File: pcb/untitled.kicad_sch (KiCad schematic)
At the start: 66 parts, among them J1 00222-32051, J10 0022-232021, J2 0022-232021, J3 0022-232041, J8 00222-32051, Q1 SI7465DP-T1-E3, U2 MP26123DR-LF-Z, U3 TPS63070

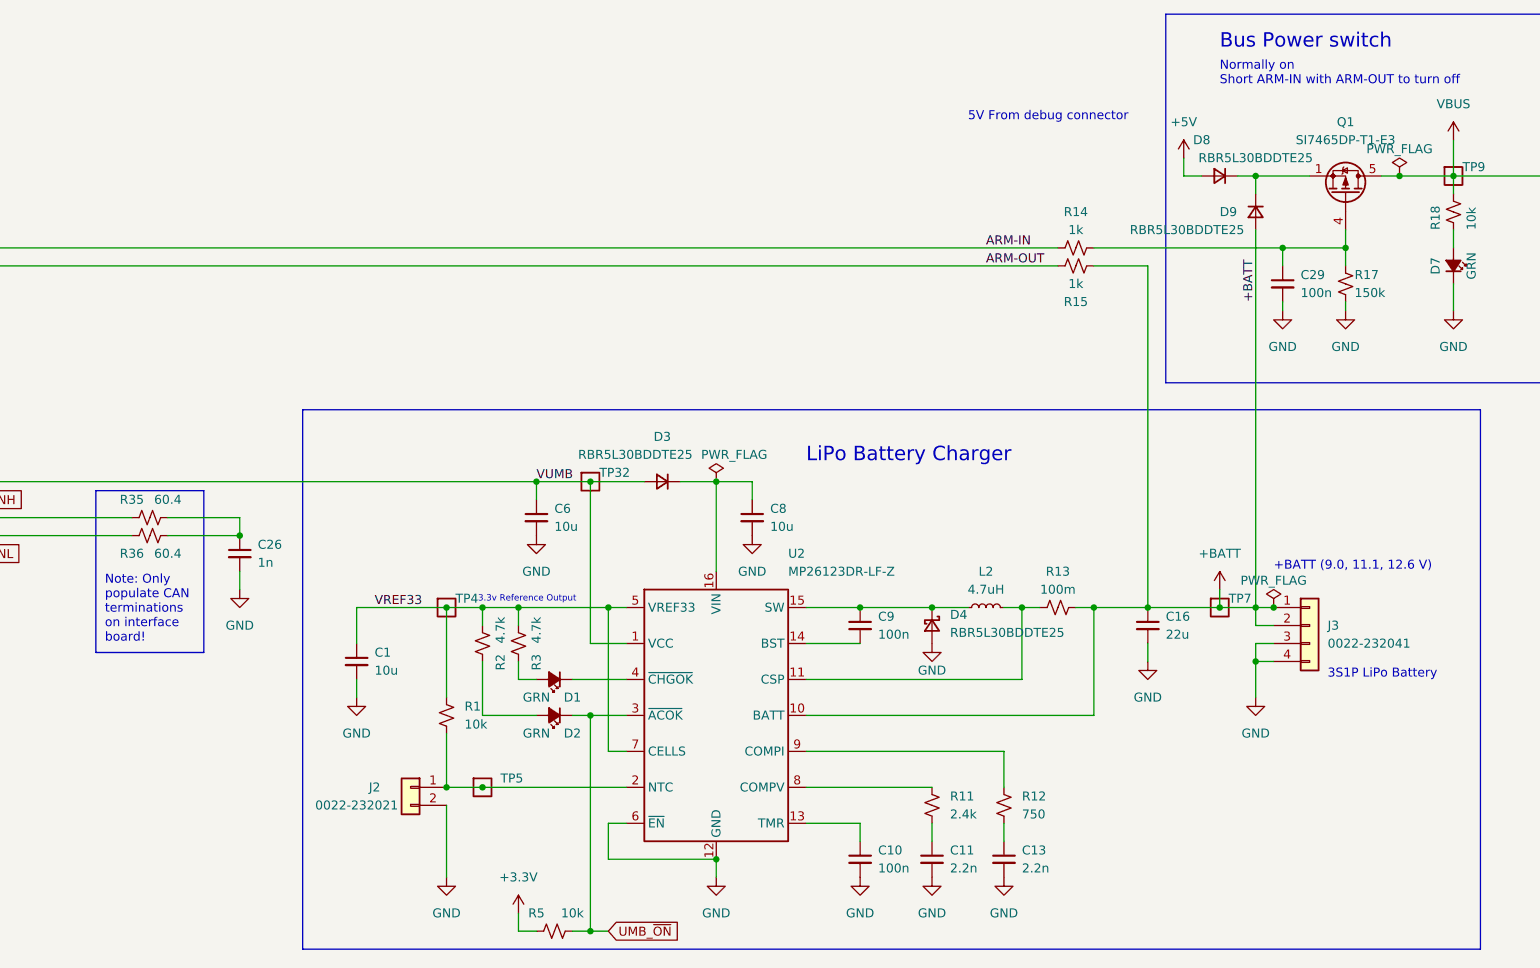
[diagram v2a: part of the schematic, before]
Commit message: Rough draft schematic, no ERC errors, ready for layout
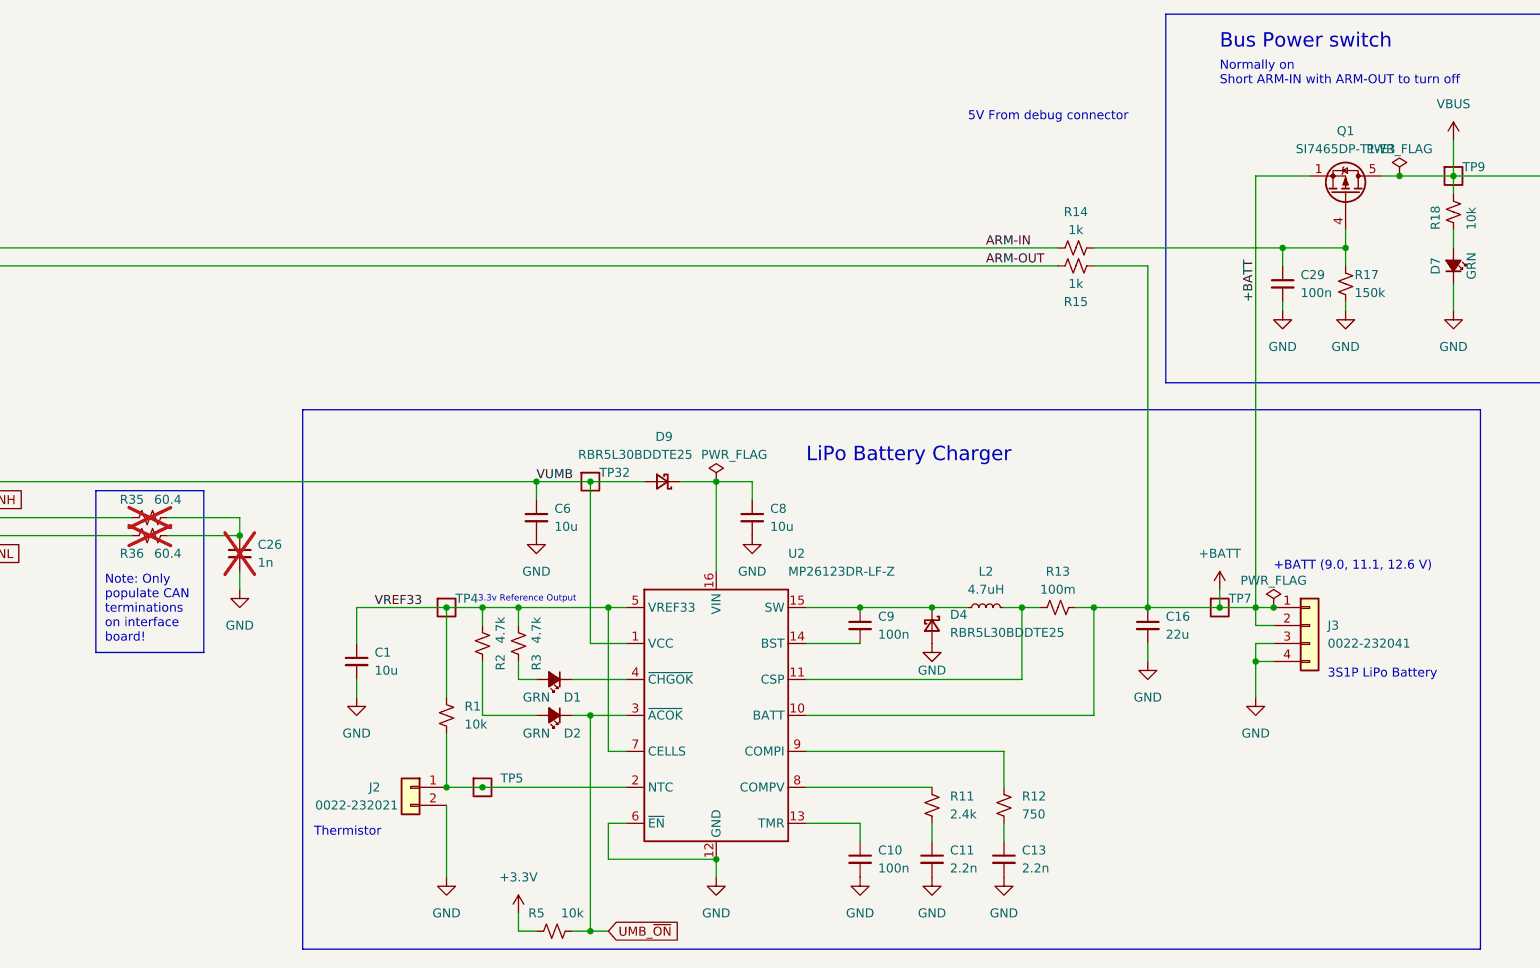
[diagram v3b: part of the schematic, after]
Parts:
- removed D3, D8, D9: RBR5L30BDDTE25, Diode_SMD:D_SMA, symbol Device:D_Small
- added D9: RBR5L30BDDTE25, Diode_SMD:D_SMA, symbol Device:D_Schottky_Small
- C26, R35, R36: now not fitted
- Q1: footprint psas-footprints:PowerPAK_SO-8_Single -> PCM_Package_SON_AKL:Infineon_PG-TDSON-8
- TP30, TP31, TP6: now left out of the parts list
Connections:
- net +BATT: now also Q1.1 (S), Q1.2 (S), Q1.3 (S)
- net VUMB: now also D9.2 (A)
- net at C8.1, U2.16 (VIN): now also D9.1 (K)
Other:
- note added: "Thermistor"
